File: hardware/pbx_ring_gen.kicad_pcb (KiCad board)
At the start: 2 copper layers, 44.4 x 99.8 mm, 18 parts, among them J1 Conn_02x02_Odd_Even, J2 Screw_Terminal_01x04, U1 PCR-SIN06

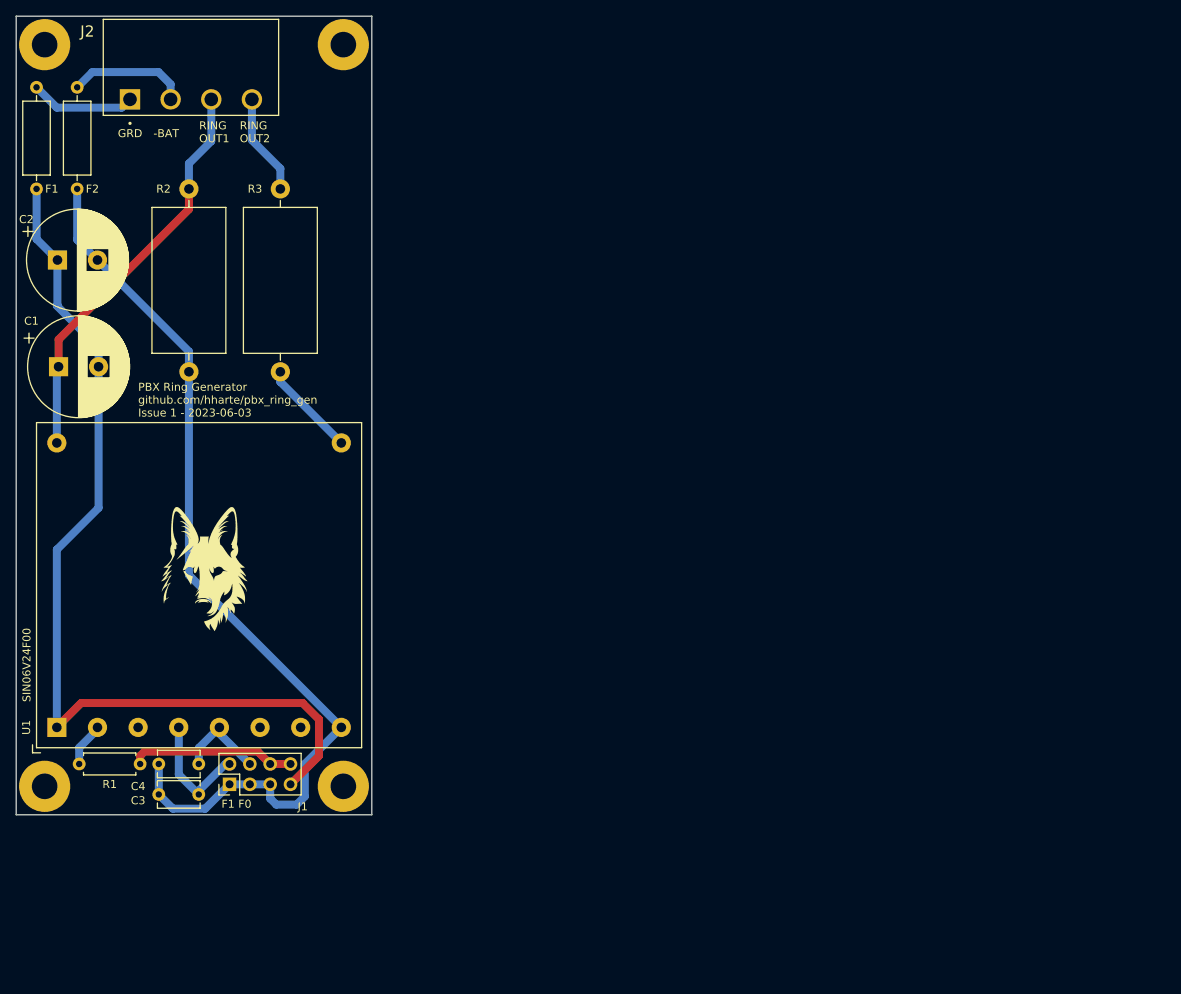
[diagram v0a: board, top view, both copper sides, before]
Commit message: Fix mirrored footprint for PCR-SIN06.
    * The footprint for the PCR-SIN06 ring generator was mirrored in the
      Issue 1 PCB.  Install the ring generator on the solder side of the
      PCB for Issue 1.
    * Corrected PCR-SIN06 footprint.
    * Added a jumper that can be cut for DC-biased ringing.
    * Update revision to Issue 2.
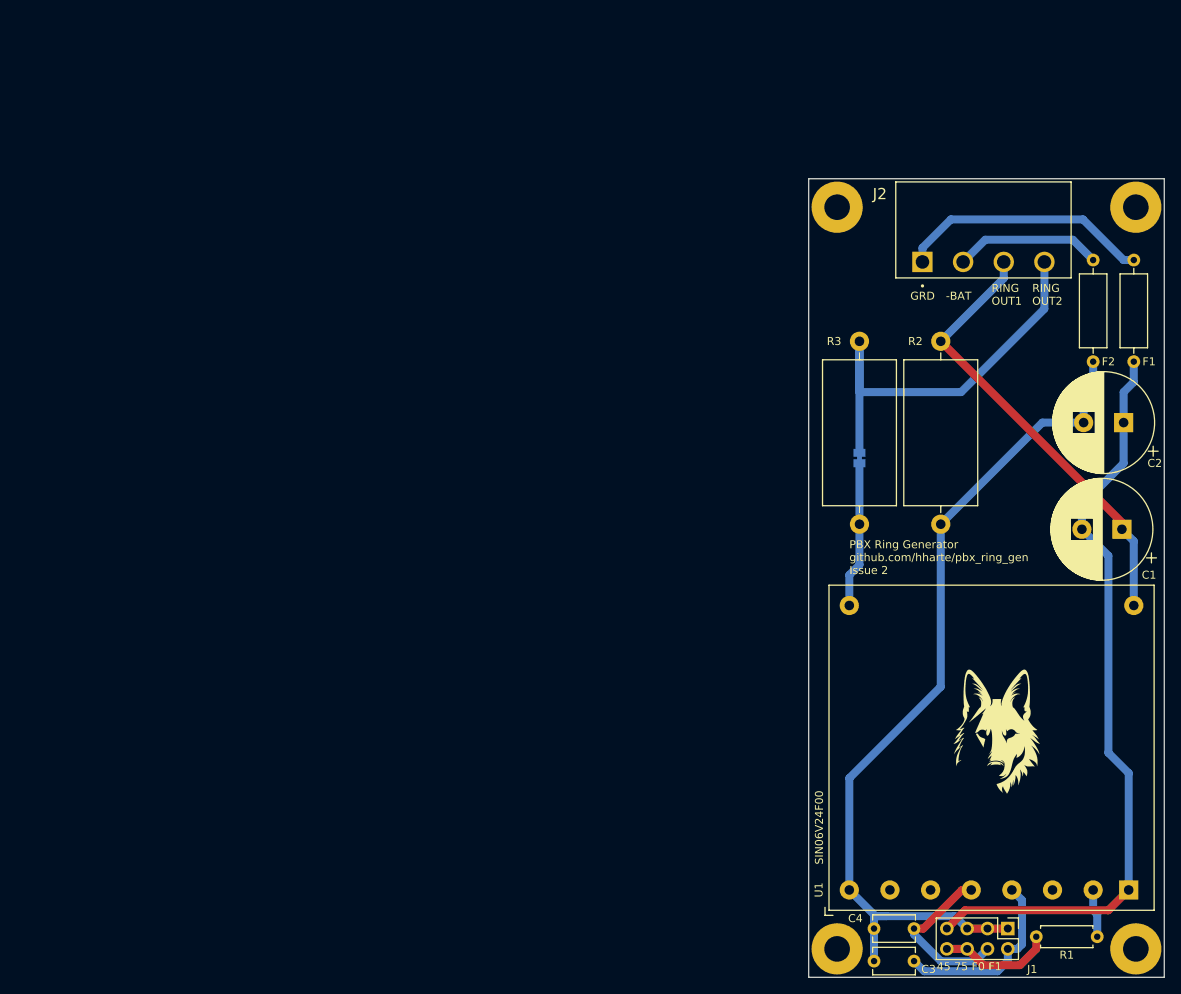
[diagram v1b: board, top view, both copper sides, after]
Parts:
- added JP1: Jumper_2_Bridged, Jumper:SolderJumper-2_P1.3mm_Bridged_Pad1.0x1.5mm, B.Cu at (138.4, 78.1)
- moved F1 138.8 mm to (172.7, 66.0)
- moved C2 134.8 mm to (171.4, 73.7), turned to 180 degrees
- moved C1 134.5 mm to (171.2, 87.0), turned to 180 degrees
- moved R1 129.1 mm to (168.1, 137.9), turned to 180 degrees
- moved F2 128.8 mm to (167.6, 66.0)
- moved Deena 103.7 mm to (158.8, 69.8)
- moved H1 101.1 mm to (135.6, 139.4)
- moved H4 101.1 mm to (135.6, 46.7)
- moved J2 101.1 mm to (146.3, 53.6)
- moved U1 101.1 mm to (137.2, 132.1)
- moved Deena 101.1 mm to (155.6, 112.4)
- moved H2 101.1 mm to (173.0, 139.4)
- moved H3 101.1 mm to (173.0, 46.7)
- moved J1 98.9 mm to (157.0, 136.9), turned to -90 degrees
- moved R2 95.9 mm to (148.6, 86.4)
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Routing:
- net /RING_OUT2: track 12.7 -> 53.6 mm
- net GNDPWR: track 117.2 -> 95.9 mm
- net /PBX_GRD: track 13.2 -> 31.8 mm
- net Net-(J1-Pin_4): track 11.8 -> 21.1 mm
- net Net-(J1-Pin_2): track 15.1 -> 23.6 mm
- net -BATT: track 118.1 -> 110.5 mm
- net Net-(J1-Pin_6): track 20.7 -> 14.4 mm
- net /RING_OUT1: track 50.9 -> 56.2 mm
- net Net-(JP1-A): track 12.0 -> 17.1 mm
- net /PBX_BATT: track 15.0 -> 18.5 mm
- net Net-(U1-OAC): track 5.52 -> 6.05 mm
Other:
- board text added: "0.2000 mm / 0.0000 mm"
- board text added: "0.3000 mm"
- board text added: "1.6000 mm"
- board text added: "2"
- board text added: "44.4500 mm x 99.8220 mm"
- board text added: "45 75 F0 F1"
- board text added: "BOARD CHARACTERISTICS"
- board text added: "Board Thickness:"
- board text added: "Board overall dimensions:"
- board text added: "Castellated pads:"
- board text added: "Copper Finish:"
- board text added: "Copper Layer Count:"
- board text added: "Edge card connectors:"
- board text added: "For DC-biased output: 1. Cut jumper JP1 2. Install C1 3. Install R2, R3 Output is RING OUT2, referenced to GRD."
- board text added: "Impedance Control:"
- board text added: "Min hole diameter:"
- board text added: "Min track/spacing:"
- board text added: "No"
- board text added: "None"
- board text added: "PBX Ring Generator github.com/hharte/pbx_ring_gen Issue 2"
- board text added: "Plated Board Edge:"
- board text removed: "F1 F0"
- board text removed: "PBX Ring Generator github.com/hharte/pbx_ring_gen Issue 1 - 2023-06-03"

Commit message: Update for KiCAD 8.0.1.
    * Update BOM.
    * Update README.md.
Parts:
- C1: value 20uF / 35V -> 22uF / 100V

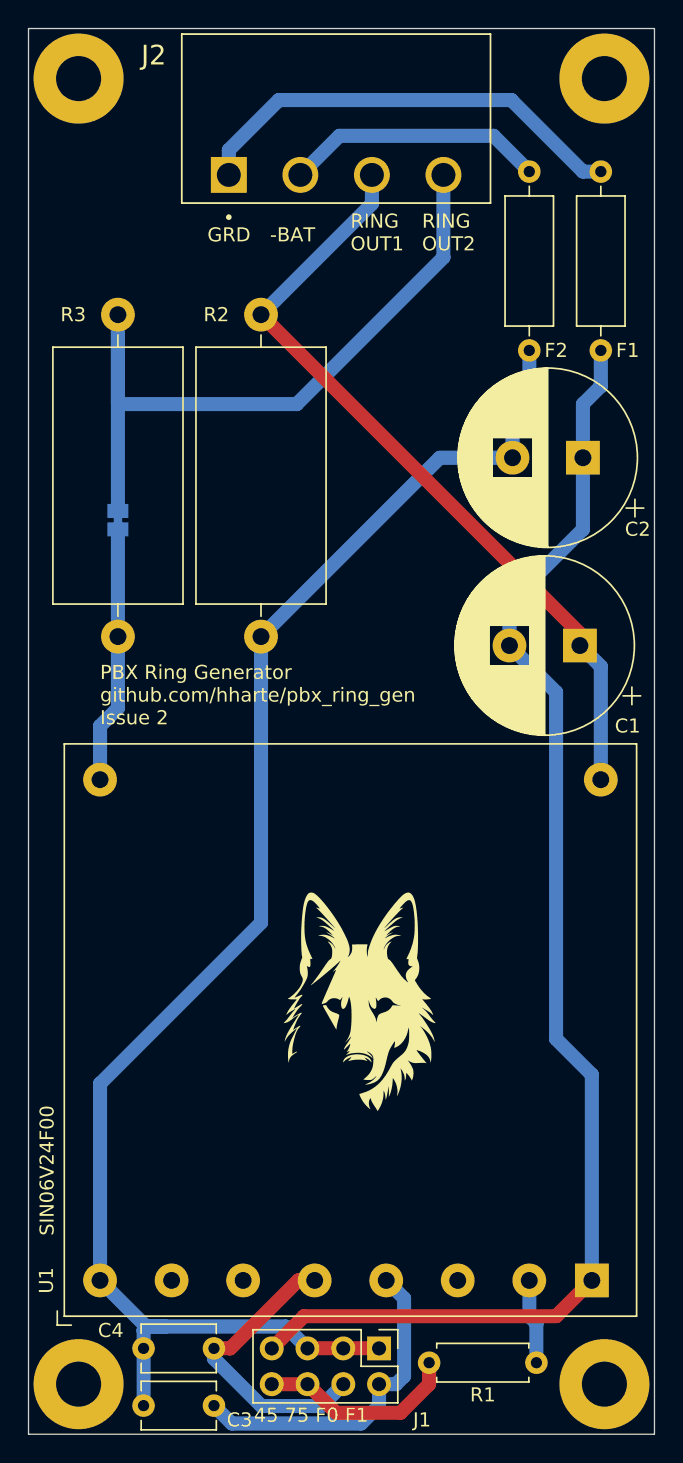
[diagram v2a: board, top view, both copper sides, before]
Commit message: Update to Rev 3.
    * Round PCB corners.
    * Move connector closer to edge.
    * Update fuses to 1.5A.
    * Create cover for the PBX ring generator.
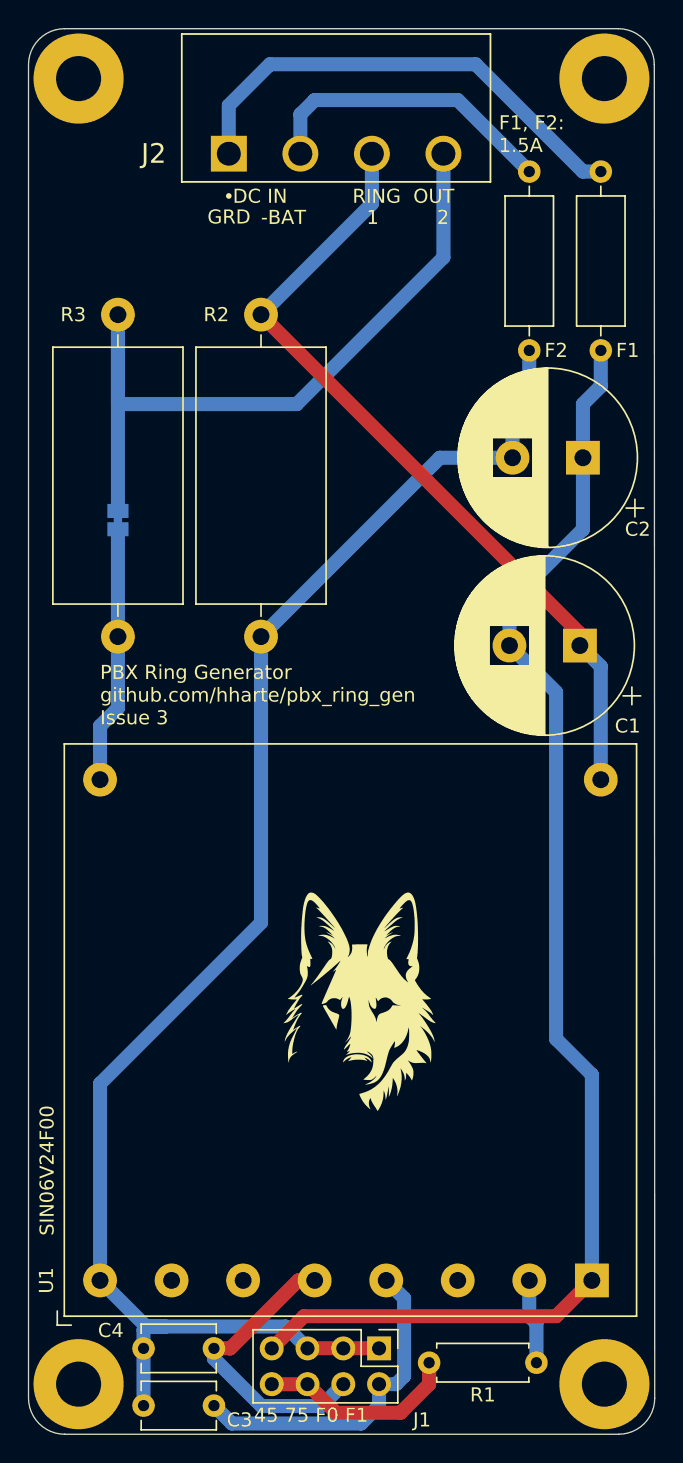
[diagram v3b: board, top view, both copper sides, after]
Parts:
- C2: value 100uF / 35V -> 100uF / 50V
- C3, C4: value 0.047uF -> 0.047uF / 50V
- F1, F2: value Fuse 630mA -> Fuse 1.5A
- J2: value Screw_Terminal_01x04 -> TBP01R1-508-04BE
- moved Deena 41.1 mm to (141.6, 107.2)
- moved J2 1.51 mm to (146.3, 52.1)
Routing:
- net /PBX_BATT: track 18.5 -> 21.6 mm
- net /PBX_GRD: track 31.8 -> 34.2 mm
- net /RING_OUT2: track 53.6 -> 55.1 mm
- net /RING_OUT1: track 56.2 -> 57.7 mm
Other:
- board size 44.4 x 99.8 mm -> 44.5 x 99.8 mm
- board text added: "1"
- board text added: "DC IN"
- board text added: "F1, F2: 1.5A"
- board text added: "For DC-biased output: 1. Cut jumper JP1 --> 2. Install C1 3. Install R2, R3 Output is RING OUT2, referenced to GRD."
- board text added: "PBX GRD: 0V PBX BATT: -24VDC RING OUT1 / OUT2: isolated output. RING OUT2: DC-Biased output (referenced to PBX GRD)"
- board text added: "PBX Ring Generator github.com/hharte/pbx_ring_gen Issue 3"
- board text added: "RING OUT"
- board text removed: "For DC-biased output: 1. Cut jumper JP1 2. Install C1 3. Install R2, R3 Output is RING OUT2, referenced to GRD."
- board text removed: "PBX GRD: 0V PBX BATT: -24VDC RING OUT1: Use for isolated output only. RING OUT2: Use for DC-Biased (referenced to PBX GRD)"
- board text removed: "PBX Ring Generator github.com/hharte/pbx_ring_gen Issue 2"
- board text removed: "RING OUT1"
- board text removed: "RING OUT2"
